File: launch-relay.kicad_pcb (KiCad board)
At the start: 2 copper layers, 1 part

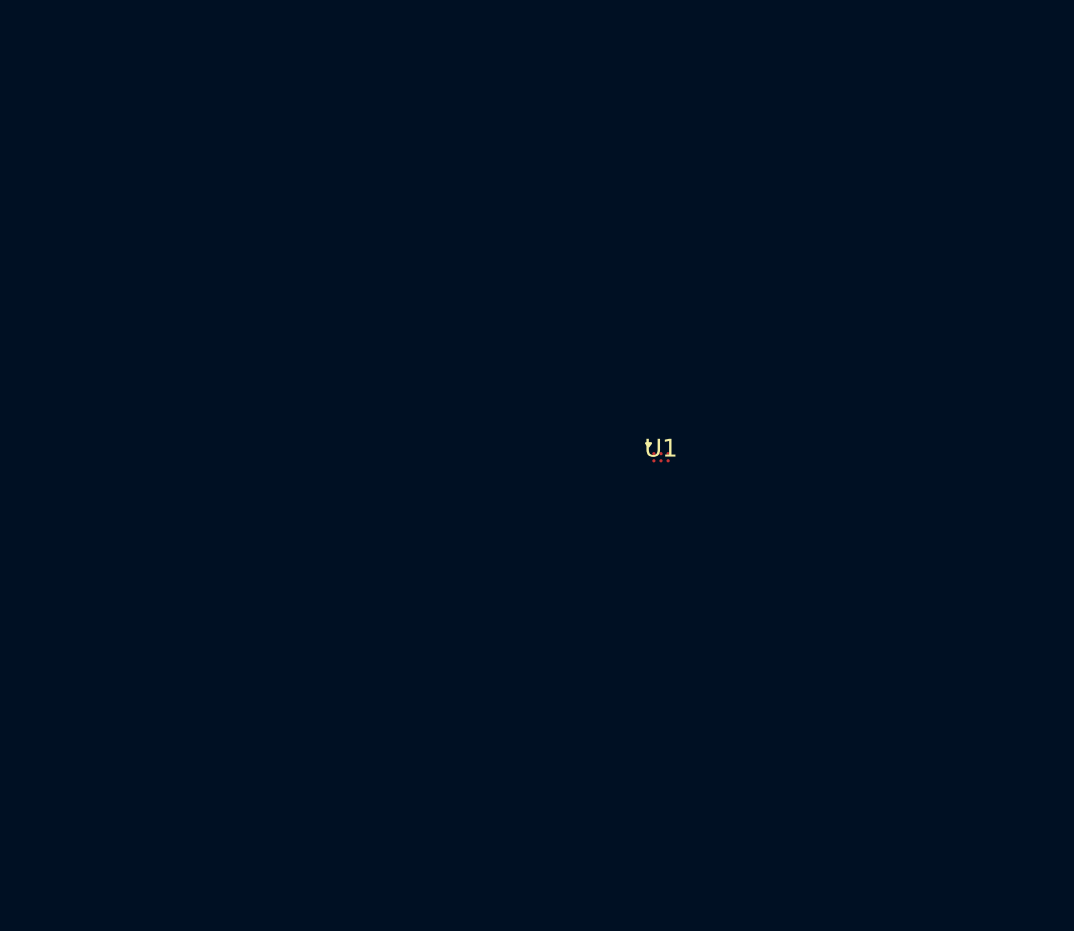
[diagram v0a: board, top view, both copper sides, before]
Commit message: finalized schematic and prepped layout
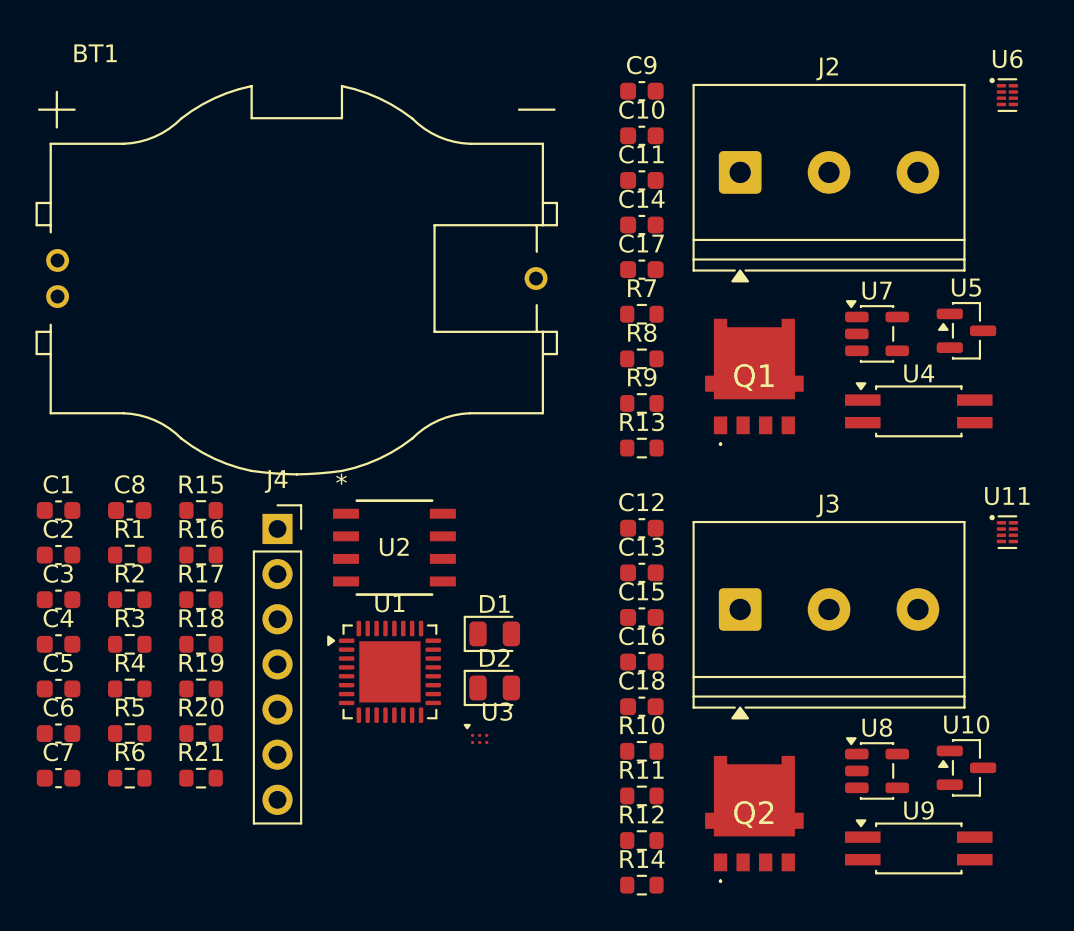
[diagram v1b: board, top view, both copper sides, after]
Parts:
- added BT1: BHSD-2032-PC, HPRC_Connectors:BAT_BHSD-2032-PC, F.Cu at (116.4, 69.3)
- added C1: 100nF, Capacitor_SMD:C_0603_1608Metric, F.Cu at (103.0, 82.3)
- added C10: 2.2u, Capacitor_SMD:C_0603_1608Metric, F.Cu at (135.8, 61.3)
- added C11: 1u, Capacitor_SMD:C_0603_1608Metric, F.Cu at (135.8, 63.8)
- added C12: 2.2u, Capacitor_SMD:C_0603_1608Metric, F.Cu at (135.8, 83.3)
- added C13: 1u, Capacitor_SMD:C_0603_1608Metric, F.Cu at (135.8, 85.9)
- added C14: 100n, Capacitor_SMD:C_0603_1608Metric, F.Cu at (135.8, 66.3)
- added C15: 100n, Capacitor_SMD:C_0603_1608Metric, F.Cu at (135.8, 88.4)
- added C16: 22p, Capacitor_SMD:C_0603_1608Metric, F.Cu at (135.8, 90.9)
- added C17: 100n, Capacitor_SMD:C_0603_1608Metric, F.Cu at (135.8, 68.8)
- added C18: 100n, Capacitor_SMD:C_0603_1608Metric, F.Cu at (135.8, 93.4)
- added C2: 100n, Capacitor_SMD:C_0603_1608Metric, F.Cu at (103.0, 84.9)
- added C3: 4.7u, Capacitor_SMD:C_0603_1608Metric, F.Cu at (103.0, 87.4)
- added C4: 100n, Capacitor_SMD:C_0603_1608Metric, F.Cu at (103.0, 89.9)
- added C5: 100n, Capacitor_SMD:C_0603_1608Metric, F.Cu at (103.0, 92.4)
- added C6: 100n, Capacitor_SMD:C_0603_1608Metric, F.Cu at (103.0, 94.9)
- added C7: 4.7u, Capacitor_SMD:C_0603_1608Metric, F.Cu at (103.0, 97.4)
- added C8: 4.7u, Capacitor_SMD:C_0603_1608Metric, F.Cu at (107.0, 82.3)
- added C9: 22p, Capacitor_SMD:C_0603_1608Metric, F.Cu at (135.8, 58.8)
- added D1: LED, LED_SMD:LED_0805_2012Metric, F.Cu at (127.5, 89.3)
- added D2: LED, LED_SMD:LED_0805_2012Metric, F.Cu at (127.5, 92.3)
- added J2: Screw_Terminal_01x03, TerminalBlock_Philmore:TerminalBlock_Philmore_TB133_1x03_P5.00mm_Horizontal, F.Cu at (141.4, 63.3)
- added J3: Screw_Terminal_01x03, TerminalBlock_Philmore:TerminalBlock_Philmore_TB133_1x03_P5.00mm_Horizontal, F.Cu at (141.4, 87.9)
- added J4: Conn_01x07_Socket, Connector_PinSocket_2.54mm:PinSocket_1x07_P2.54mm_Vertical, F.Cu at (115.3, 83.4)
- added Q1: NVMFS5C460NLAFT1G-YE, HPRC_Logic:NVMFS3D0P04M8LT1G, F.Cu at (142.2, 74.8)
- added Q2: NVMFS5C460NLAFT1G-YE, HPRC_Logic:NVMFS3D0P04M8LT1G, F.Cu at (142.2, 99.3)
- added R1: 10k, Resistor_SMD:R_0603_1608Metric, F.Cu at (107.0, 84.9)
- added R10: 1k, Resistor_SMD:R_0603_1608Metric, F.Cu at (135.8, 95.9)
- added R11: 1k, Resistor_SMD:R_0603_1608Metric, F.Cu at (135.8, 98.4)
- added R12: 10k, Resistor_SMD:R_0603_1608Metric, F.Cu at (135.8, 100.9)
- added R13: 330, Resistor_SMD:R_0603_1608Metric, F.Cu at (135.8, 78.8)
- added R14: 330, Resistor_SMD:R_0603_1608Metric, F.Cu at (135.8, 103.4)
- added R15: 0, Resistor_SMD:R_0603_1608Metric, F.Cu at (111.0, 82.3)
- added R16: 0, Resistor_SMD:R_0603_1608Metric, F.Cu at (111.0, 84.9)
- added R17: 0, Resistor_SMD:R_0603_1608Metric, F.Cu at (111.0, 87.4)
- added R18: 0, Resistor_SMD:R_0603_1608Metric, F.Cu at (111.0, 89.9)
- added R19: 0, Resistor_SMD:R_0603_1608Metric, F.Cu at (111.0, 92.4)
- added R2: 10k, Resistor_SMD:R_0603_1608Metric, F.Cu at (107.0, 87.4)
- added R20: 10k, Resistor_SMD:R_0603_1608Metric, F.Cu at (111.0, 94.9)
- added R21: 10k, Resistor_SMD:R_0603_1608Metric, F.Cu at (111.0, 97.4)
- added R3: 2.2k, Resistor_SMD:R_0603_1608Metric, F.Cu at (107.0, 89.9)
- added R4: 2.2k, Resistor_SMD:R_0603_1608Metric, F.Cu at (107.0, 92.4)
- added R5: 10k, Resistor_SMD:R_0603_1608Metric, F.Cu at (107.0, 94.9)
- added R6: 10k, Resistor_SMD:R_0603_1608Metric, F.Cu at (107.0, 97.4)
- added R7: 1k, Resistor_SMD:R_0603_1608Metric, F.Cu at (135.8, 71.3)
- added R8: 1k, Resistor_SMD:R_0603_1608Metric, F.Cu at (135.8, 73.8)
- added R9: 10k, Resistor_SMD:R_0603_1608Metric, F.Cu at (135.8, 76.3)
- added U10: TPS3839DBZ, Package_TO_SOT_SMD:SOT-23, F.Cu at (154.1, 96.8)
- added U11: SN74LVC1G74DQER, Package_SON:X2SON-8_1.4x1mm_P0.35mm, F.Cu at (156.4, 83.6)
- added U2: MX25R3235FM1IL0, HPRC_Storage:SOP_8L_150_MAC, F.Cu at (121.9, 84.4)
- added U3: BMA580, HPRC_Sensors:BMA580, F.Cu at (126.7, 95.2)
- added U4: ACPL-217, Package_SO:SO-4_4.4x2.3mm_P1.27mm, F.Cu at (151.4, 76.8)
- added U5: TPS3839DBZ, Package_TO_SOT_SMD:SOT-23, F.Cu at (154.1, 72.2)
- added U6: SN74LVC1G74DQER, Package_SON:X2SON-8_1.4x1mm_P0.35mm, F.Cu at (156.4, 59.0)
- added U7: TPS7A2433DBVR, Package_TO_SOT_SMD:SOT-23-5, F.Cu at (149.1, 72.4)
- added U8: TPS7A2433DBVR, Package_TO_SOT_SMD:SOT-23-5, F.Cu at (149.1, 97.0)
- added U9: ACPL-217, Package_SO:SO-4_4.4x2.3mm_P1.27mm, F.Cu at (151.4, 101.4)
- U1: value ~ -> STM32U083KCUx; footprint sensors:BMA580 -> Package_DFN_QFN:QFN-32-1EP_5x5mm_P0.5mm_EP3.45x3.45mm
- moved U1 19.5 mm to (121.7, 91.4)
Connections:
- U1 pad 1: unconnected-(U1-VDD-Pad1) -> +3V0
- U1 pad 5: unconnected-(U1-SCL-Pad5) -> +3V0

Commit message: setup 6 layer board
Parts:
- moved C10 45.6 mm to (179.6, 48.7)
- moved C11 45.6 mm to (179.6, 51.2)
- moved C13 45.6 mm to (179.6, 73.3)
- moved C17 45.6 mm to (179.6, 56.3)
- moved C18 45.6 mm to (179.6, 80.9)
- moved C9 45.6 mm to (179.6, 46.2)
- moved J2 45.6 mm to (185.2, 50.8)
- moved J3 45.6 mm to (185.2, 75.4)
- moved R12 45.6 mm to (179.6, 88.4)
- moved R7 45.6 mm to (179.6, 58.8)
- moved R9 45.6 mm to (179.6, 63.8)
- moved U6 45.6 mm to (200.2, 46.4)
- moved C12 45.6 mm to (179.6, 70.8)
- moved C14 45.6 mm to (179.6, 53.8)
- moved C15 45.6 mm to (179.6, 75.8)
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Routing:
- added copper zone on In2.Cu, net +3V0
- added copper zone on In1.Cu, net GND
- added copper zone on In4.Cu, net GND
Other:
- board outline added: 50 x 50 mm
- copper layers 2 -> 6

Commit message: Payload PCB
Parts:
- BT1, Q1, Q2: moved to B.Cu
- moved U5 178.1 mm to (20.4, 44.6)
- moved U6 176.0 mm to (24.3, 42.1), turned to -90 degrees
- moved J2 166.2 mm to (19.0, 53.3), turned to -90 degrees
- moved U7 165.2 mm to (28.3, 45.6), turned to 180 degrees
- moved C17 163.2 mm to (16.9, 44.5), turned to -90 degrees
- moved U9 162.0 mm to (39.7, 43.5), turned to 90 degrees
- moved U4 161.6 mm to (35.0, 43.6), turned to -90 degrees
- moved R13 160.8 mm to (20.9, 40.2)
- moved C14 160.0 mm to (19.8, 48.9), turned to 180 degrees
- moved C9 158.9 mm to (20.9, 38.4)
- moved R9 157.4 mm to (24.4, 37.9)
- moved Q1 157.3 mm to (28.7, 57.0)
- moved C10 154.6 mm to (25.1, 45.6), turned to 90 degrees
- moved D2 153.3 mm to (30.6, 19.1)
- moved U2 152.3 mm to (20.5, 26.0), turned to 180 degrees
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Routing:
- net GND: track 0.00 -> 87.1 mm, vias 0 -> 7
- net +3V0: track 0.00 -> 55.1 mm, vias 0 -> 8
- net /Circuit Switch1/BATT_GND: track 0.00 -> 49.0 mm, vias 0 -> 3
- net /Circuit Switch2/BATT_GND: track 0.00 -> 36.5 mm, vias 0 -> 2
- net /Circuit Switch1/3.3V_BATT: track 0.00 -> 35.1 mm, vias 0 -> 2
- net /Circuit Switch2/3.3V_BATT: track 0.00 -> 34.5 mm
- net /SPI3_MOSI: track 0.00 -> 21.0 mm
- net /Flash_CS: track 0.00 -> 20.6 mm
- net /USART1_RX: track 0.00 -> 19.0 mm
- net /DUMP: track 0.00 -> 18.7 mm
- net /Switch2: track 0.00 -> 16.9 mm, vias 0 -> 2
- net /SPI3_SCK: track 0.00 -> 15.4 mm
- net Net-(U10-~{RESET}): track 0.00 -> 15.3 mm, vias 0 -> 2
- net /I2C2_SDA: track 0.00 -> 14.7 mm
- net /Switch1: track 0.00 -> 14.6 mm
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- added copper zone on In1.Cu, net /Circuit Switch1/BATT_GND
- added copper zone on In4.Cu, net /Circuit Switch1/BATT_GND
- added copper zone on In1.Cu, net /Circuit Switch2/BATT_GND
- added copper zone on In4.Cu, net /Circuit Switch2/BATT_GND
- added copper zone on In1.Cu, net /DEBUG_JTCK-SWCLK
- added copper zone on In4.Cu, net /DEBUG_JTCK-SWCLK
- removed copper zone on In1.Cu, net GND
- removed copper zone on In4.Cu, net GND
